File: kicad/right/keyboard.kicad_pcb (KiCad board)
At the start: 2 copper layers, 141 x 130.1 mm, 70 parts

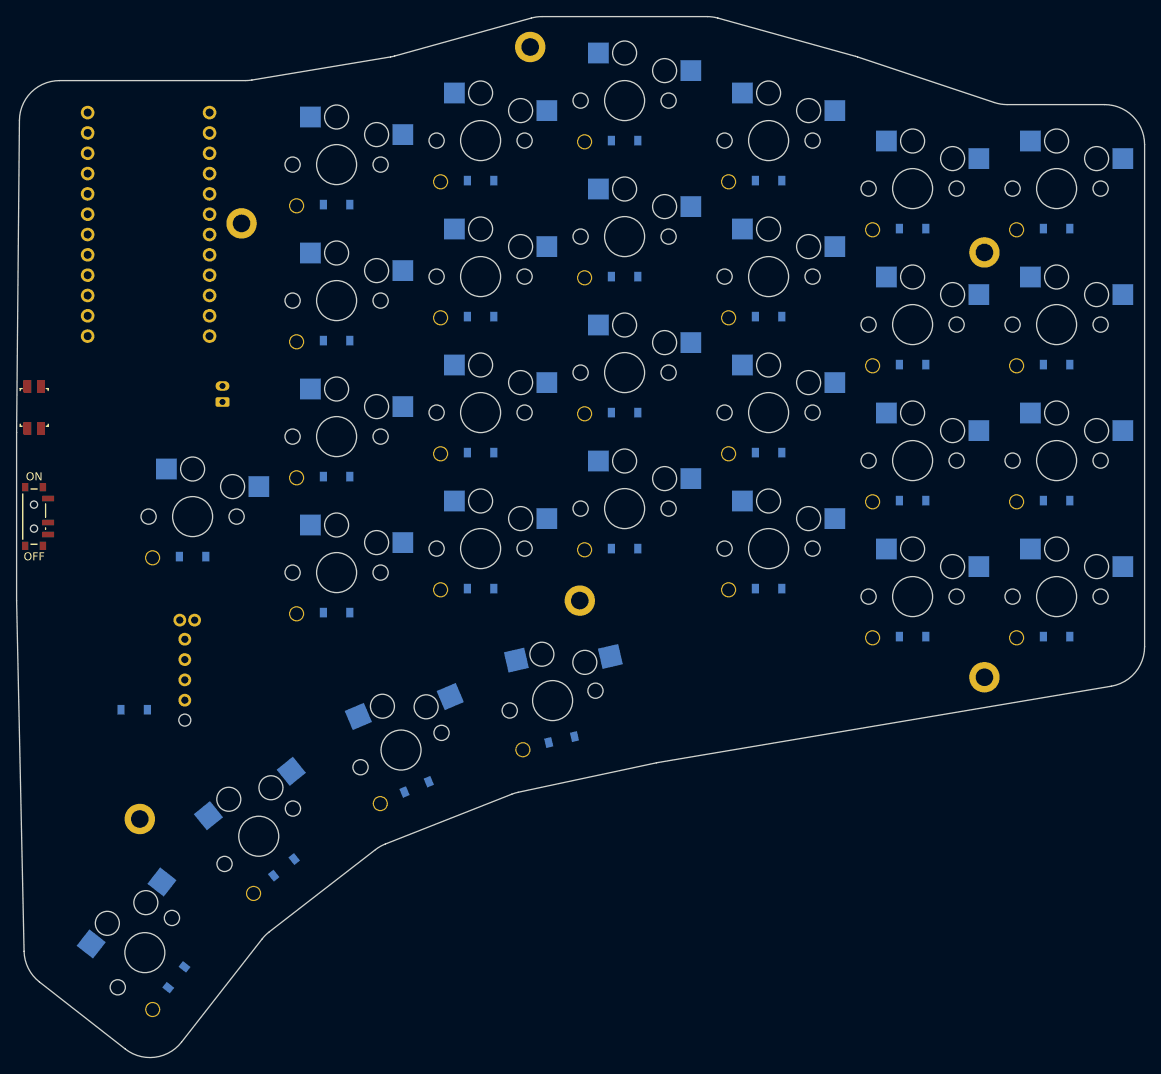
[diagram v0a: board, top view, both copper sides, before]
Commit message: Route right half; add F.Cu GND pour, remove dangling stub
- Right half fully routed (1279 tracks, 178 vias), 0 unconnected, 0 DRC errors.
- Removed a 0.1mm dangling track stub on P16 left by the router.
- Added an F.Cu GND pour to match the left's both-sides ground, refilled zones.
- Full electrical re-audit passed: 29 switches/30 diodes, 0 matrix errors,
  MCU pin map complete, encoder push-switch wired, power chain intact.
- Gitignore KiCad .history extension folder.

Both halves are now routed and JLCPCB-manufacturable.
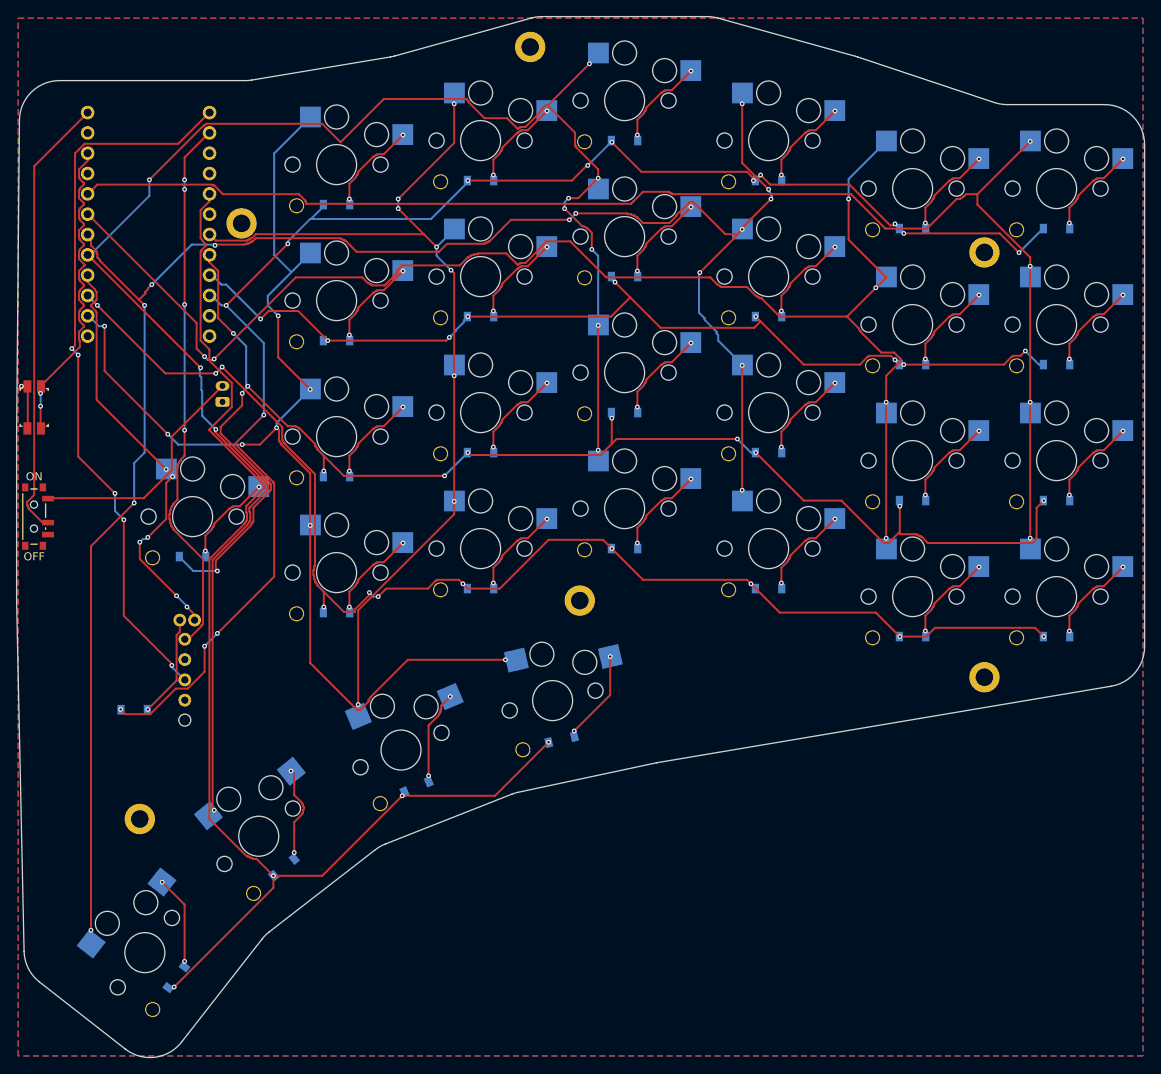
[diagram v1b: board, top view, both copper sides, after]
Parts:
- turned RST1 to 90 degrees
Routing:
- net P19: track 0.00 -> 236.8 mm, vias 0 -> 14
- net P18: track 0.00 -> 216.1 mm, vias 0 -> 11
- net P11: track 0.00 -> 191.3 mm, vias 0 -> 14
- net P13: track 0.00 -> 182.1 mm, vias 0 -> 12
- net P20: track 0.00 -> 181.3 mm, vias 0 -> 6
- net P21: track 0.00 -> 176.6 mm, vias 0 -> 4
- net P14: track 0.00 -> 161.2 mm, vias 0 -> 11
- net P2: track 0.00 -> 160.4 mm, vias 0 -> 4
- net P16: track 0.00 -> 146.6 mm, vias 0 -> 8
- net P12: track 0.00 -> 122.2 mm, vias 0 -> 9
- net P17: track 0.00 -> 120.7 mm, vias 0 -> 8
- net ENC1_C: track 0.00 -> 90.7 mm, vias 0 -> 5
- net ENC1_A: track 0.00 -> 68.4 mm, vias 0 -> 4
- net RAW: track 0.00 -> 55.9 mm
- net P15: track 0.00 -> 52.6 mm, vias 0 -> 6
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- added copper zone on B.Cu, net GND
- added copper zone on F.Cu, net GND

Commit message: Re-route right half: cleaner 119-via route, fully DRC-clean
Re-routed with balanced layers + 0.3mm edge clearance in the routing plugin
(122 vias), then fixed the outer-column (P19) rail hugging the slanted top
edge via a targeted CLI re-route at 0.6mm edge clearance, and removed a
dangling P19 stub.

Result: 119 vias (down from 178), 0 DRC errors, 0 warnings, 0 unconnected.
Full electrical audit passes: 29 switches / 0 matrix errors, 30 diodes,
MCU pin map complete, encoder push-switch wired, power chain intact,
GND pour on both layers. JLCPCB-manufacturable.
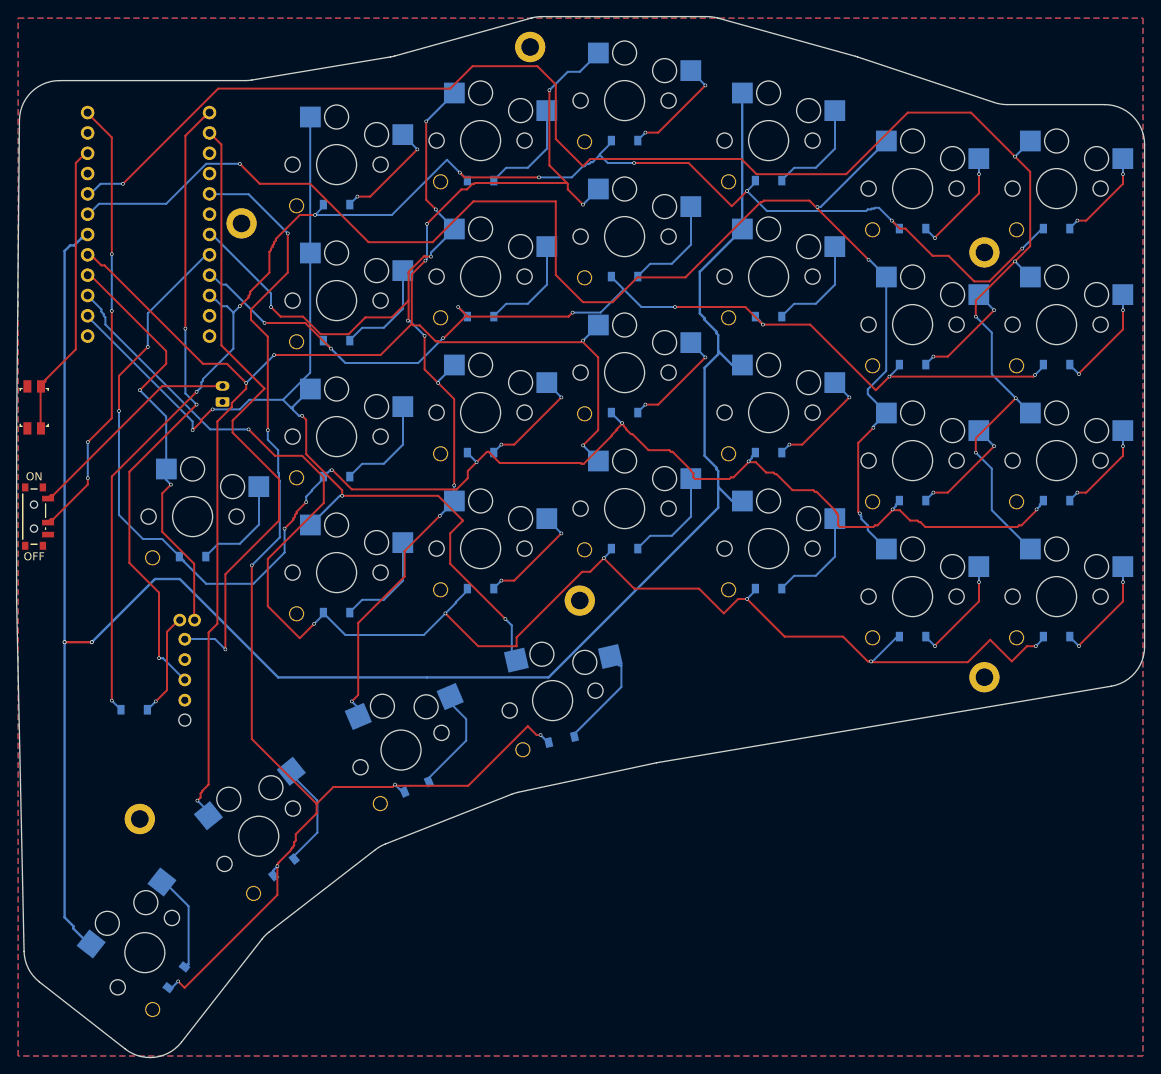
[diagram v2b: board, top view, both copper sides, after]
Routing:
- net P14: track 161.2 -> 191.5 mm, vias 11 -> 7
- net P21: track 176.6 -> 206.0 mm, vias 4 -> 6
- net P19: track 236.8 -> 255.0 mm, vias 14 -> 2
- net P16: track 146.6 -> 131.9 mm, vias 8 -> 5
- net ENC1_C: track 90.7 -> 78.5 mm, vias 5 -> 3
- net ENC1_A: track 68.4 -> 79.8 mm, vias 4 -> 1
- net P12: track 122.2 -> 129.6 mm
- net P13: track 182.1 -> 189.5 mm, vias 12 -> 10
- net P17: track 120.7 -> 127.6 mm, vias 8 -> 10
- net GND: track 6.51 -> 0.00 mm, vias 1 -> 0
- net P18: track 216.1 -> 209.9 mm, vias 11 -> 9
- net RST: track 41.1 -> 36.8 mm, vias 2 -> 0
- net P11: track 191.3 -> 194.2 mm, vias 14 -> 10
- net BAT_P: track 30.1 -> 27.7 mm
- net mirror_pinky_home: track 12.1 -> 14.2 mm
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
